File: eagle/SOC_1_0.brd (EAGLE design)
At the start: 50 x 50 mm, 16 parts, among them X1 A, X2 B, X3 X, X4 Y

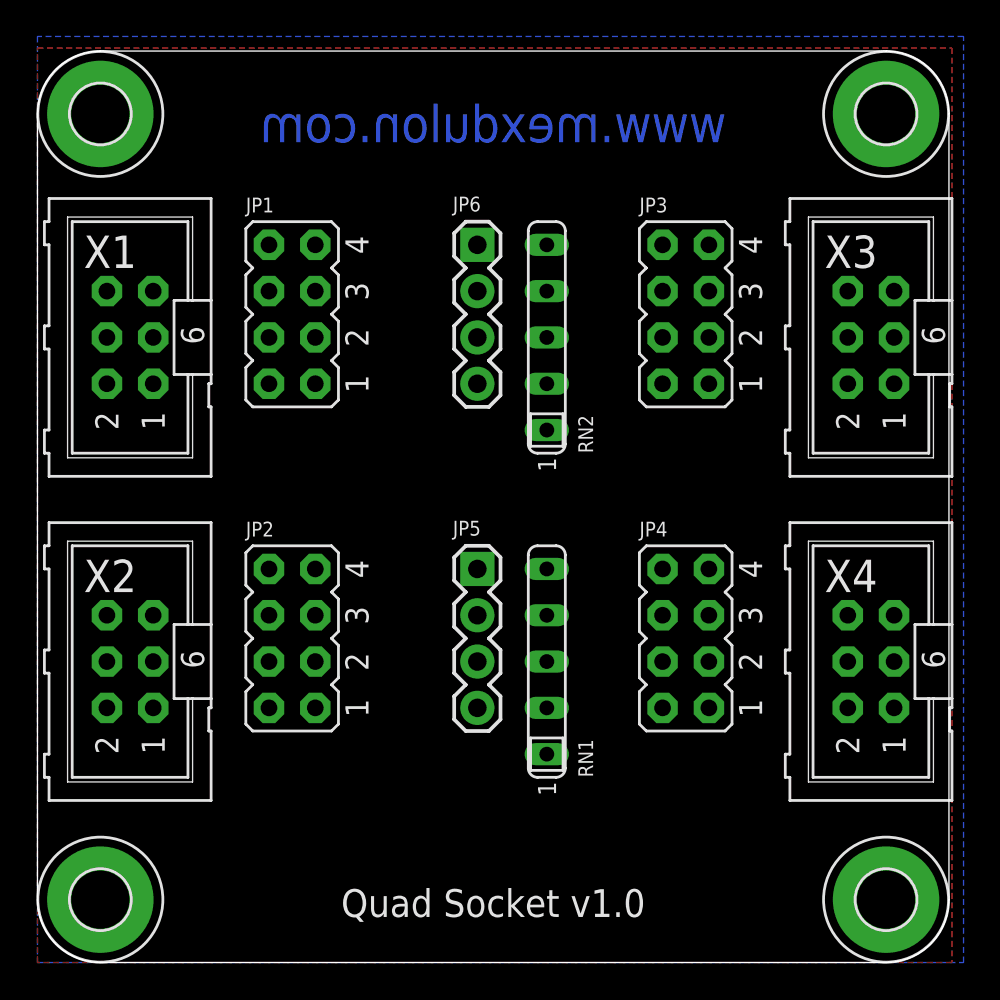
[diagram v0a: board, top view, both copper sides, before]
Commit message: New boards: eagle files (sch, brd) +ALU_1_0, CNT_1_1, D12_1_0, D14_1_0, D18_1_0, DIP_1_0, M81_1_0, N33_1_0, SWI_1_1 *SOC_1_0 modified
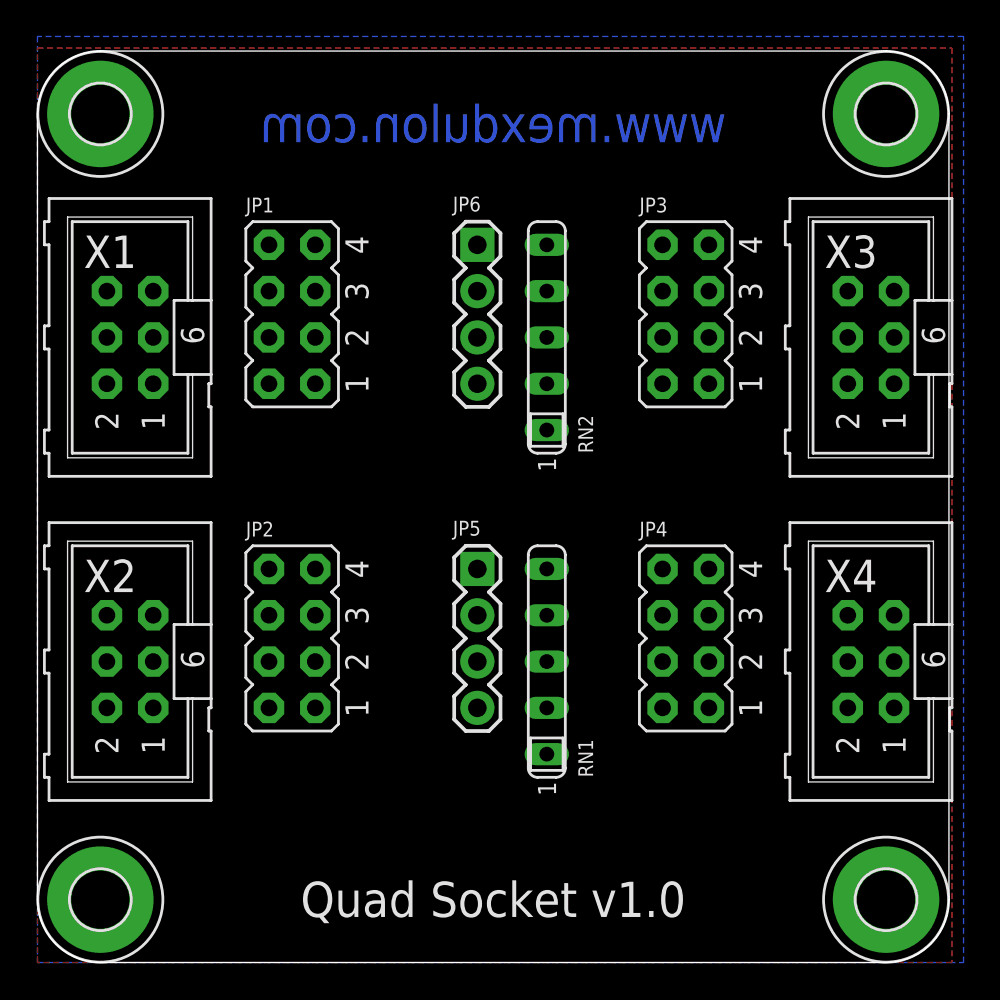
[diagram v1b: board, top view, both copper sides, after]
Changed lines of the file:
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@@
 <layer number="18" name="Vias" color="2" fill="1" visible="no" active="yes"/>
 <layer number="19" name="Unrouted" color="6" fill="1" visible="no" active="yes"/>
-<layer number="20" name="Dimension" color="15" fill="1" visible="yes" active="yes"/>
-<layer number="21" name="tPlace" color="7" fill="1" visible="yes" active="yes"/>
+<layer number="20" name="Dimension" color="15" fill="1" visible="no" active="yes"/>
+<layer number="21" name="tPlace" color="7" fill="1" visible="no" active="yes"/>
 <layer number="22" name="bPlace" color="7" fill="1" visible="no" active="yes"/>
 <layer number="23" name="tOrigins" color="15" fill="1" visible="no" active="yes"/>
 <layer number="24" name="bOrigins" color="15" fill="1" visible="no" active="yes"/>
-<layer number="25" name="tNames" color="7" fill="1" visible="yes" active="yes"/>
+<layer number="25" name="tNames" color="7" fill="1" visible="no" active="yes"/>
 <layer number="26" name="bNames" color="7" fill="1" visible="no" active="yes"/>
-<layer number="27" name="tValues" color="7" fill="1" visible="yes" active="yes"/>
+<layer number="27" name="tValues" color="7" fill="1" visible="no" active="yes"/>
 <layer number="28" name="bValues" color="7" fill="1" visible="no" active="yes"/>
 <layer number="29" name="tStop" color="7" fill="3" visible="no" active="yes"/>
@@
 <board>
 <plain>
-<text x="25" y="2.5" size="1.524" layer="25" font="vector" ratio="15" align="bottom-center">Quad Socket v1.0</text>
+<text x="25" y="2.5" size="1.9304" layer="25" font="vector" ratio="15" align="bottom-center">Quad Socket v1.0</text>
 <wire x1="0" y1="3.45" x2="0" y2="46.55" width="0" layer="20"/>
 <wire x1="3.45" y1="50" x2="46.55" y2="50" width="0" layer="20"/>
@@
 <wire x1="46.55" y1="50" x2="50" y2="46.55" width="0" layer="20" curve="-90"/>
 <wire x1="3.45" y1="50" x2="0" y2="46.55" width="0" layer="20" curve="90"/>
-<text x="25" y="45" size="2.032" layer="16" font="vector" rot="MR0" align="bottom-center">www.mexdulon.com</text>
-<text x="25" y="2.5" size="1.27" layer="26" font="vector" rot="MR0" align="bottom-center">Licensed under CERN OHL v.1.2</text>
-<text x="25" y="45" size="2.032" layer="26" font="vector" rot="MR0" align="bottom-center">www.mexdulon.com</text>
+<text x="25" y="45" size="2.032" layer="16" font="vector" ratio="12" rot="MR0" align="bottom-center">www.mexdulon.com</text>
+<text x="25" y="2.5" size="1.27" layer="26" font="vector" ratio="10" rot="MR0" align="bottom-center">Licensed under CERN OHL v.1.2</text>
+<text x="25" y="45" size="2.032" layer="26" font="vector" ratio="12" rot="MR0" align="bottom-center">www.mexdulon.com</text>
 </plain>
 <attributes>
@@
 <element name="X1" library="01-my-con" package="ML-6" value="A" x="5.08" y="34.29" smashed="yes" rot="R90">
 <attribute name="NAME" x="2.54" y="38.1" size="1.778" layer="25" font="vector"/>
-<attribute name="VALUE" x="13.97" y="29.21" size="1.778" layer="27" font="vector" rot="R180" align="bottom-center"/>
+<attribute name="VALUE" x="13.97" y="29.21" size="1.778" layer="27" font="vector" ratio="12" rot="R180" align="bottom-center"/>
 </element>
 <element name="X3" library="01-my-con" package="ML-6" value="X" x="45.72" y="34.29" smashed="yes" rot="R90">
 <attribute name="NAME" x="43.18" y="38.1" size="1.778" layer="25" font="vector"/>
-<attribute name="VALUE" x="35.56" y="29.21" size="1.778" layer="27" font="vector" rot="R180" align="bottom-center"/>
+<attribute name="VALUE" x="35.56" y="29.21" size="1.778" layer="27" font="vector" ratio="12" rot="R180" align="bottom-center"/>
 </element>
 <element name="H1" library="holes" package="3,2-PAD" value="MOUNT-PAD-ROUND3.2" x="3.45" y="3.45"/>
@@
 <element name="X2" library="01-my-con" package="ML-6" value="B" x="5.08" y="16.51" smashed="yes" rot="R90">
 <attribute name="NAME" x="2.54" y="20.32" size="1.778" layer="25" font="vector"/>
-<attribute name="VALUE" x="13.97" y="11.43" size="1.778" layer="27" font="vector" rot="R180" align="bottom-center"/>
+<attribute name="VALUE" x="13.97" y="11.43" size="1.778" layer="27" font="vector" ratio="12" rot="R180" align="bottom-center"/>
 </element>
 <element name="X4" library="01-my-con" package="ML-6" value="Y" x="45.72" y="16.51" smashed="yes" rot="R90">
 <attribute name="NAME" x="43.18" y="20.32" size="1.778" layer="25" font="vector"/>
-<attribute name="VALUE" x="35.56" y="11.43" size="1.778" layer="27" font="vector" rot="R180" align="bottom-center"/>
+<attribute name="VALUE" x="35.56" y="11.43" size="1.778" layer="27" font="vector" ratio="12" rot="R180" align="bottom-center"/>
 </element>
 <element name="JP5" library="SparkFun-Connectors" package="1X04" value="LOW" x="24.13" y="21.59" smashed="yes" rot="R270">
 <attribute name="NAME" x="22.7838" y="23.4188" size="0.8128" layer="25" font="vector" ratio="10"/>
-<attribute name="VALUE" x="25.4" y="11.43" size="1.27" layer="27" font="vector" ratio="10" rot="R180"/>
+<attribute name="VALUE" x="25.4" y="11.43" size="1.27" layer="27" font="vector" ratio="12" rot="R180"/>
 </element>
 <element name="JP6" library="SparkFun-Connectors" package="1X04" value="HIGH" x="24.13" y="39.37" smashed="yes" rot="R270">
 <attribute name="NAME" x="22.7838" y="41.1988" size="0.8128" layer="25" font="vector" ratio="10"/>
-<attribute name="VALUE" x="25.4" y="29.21" size="1.27" layer="27" font="vector" ratio="10" rot="R180"/>
+<attribute name="VALUE" x="25.4" y="29.21" size="1.27" layer="27" font="vector" ratio="12" rot="R180"/>
 </element>
 <element name="JP1" library="01-my-jumper" package="JP4Q" value="A" x="13.97" y="35.56" smashed="yes" rot="R90">
